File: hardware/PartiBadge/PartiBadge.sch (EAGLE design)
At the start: 20 parts, among them J1 I2C, J2 Supply

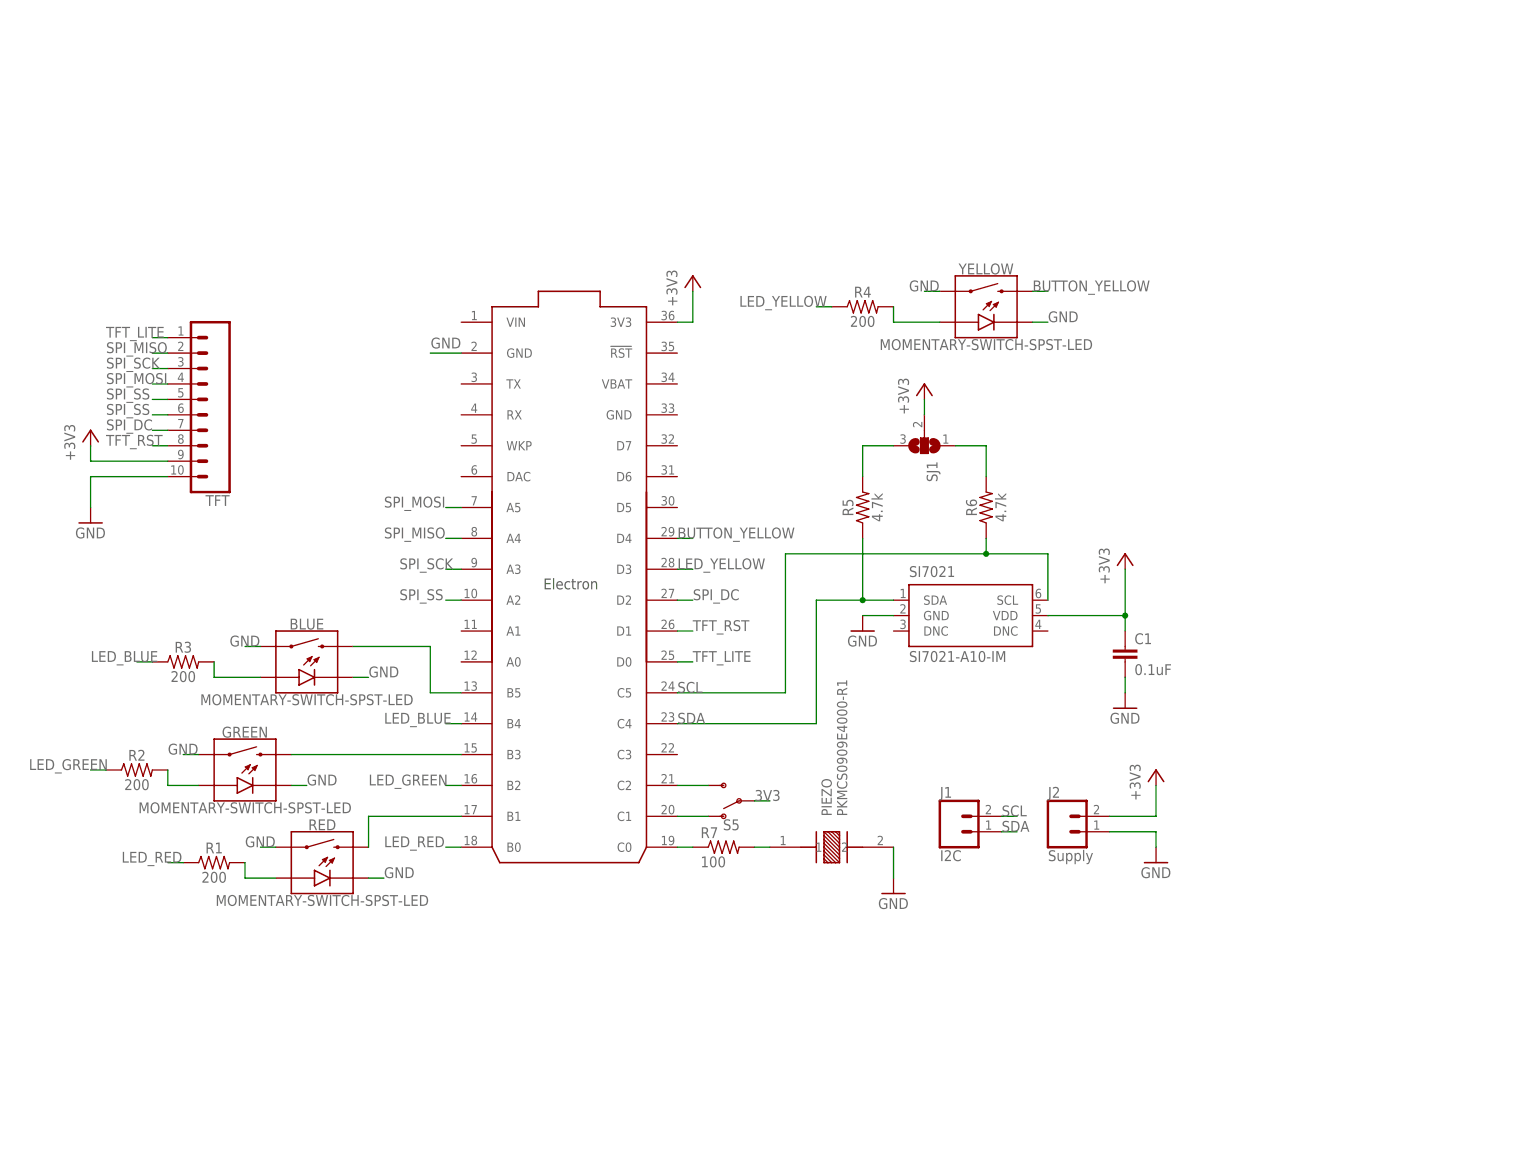
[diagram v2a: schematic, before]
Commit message: added frame and cleaned up schematic; added 5-way joystick
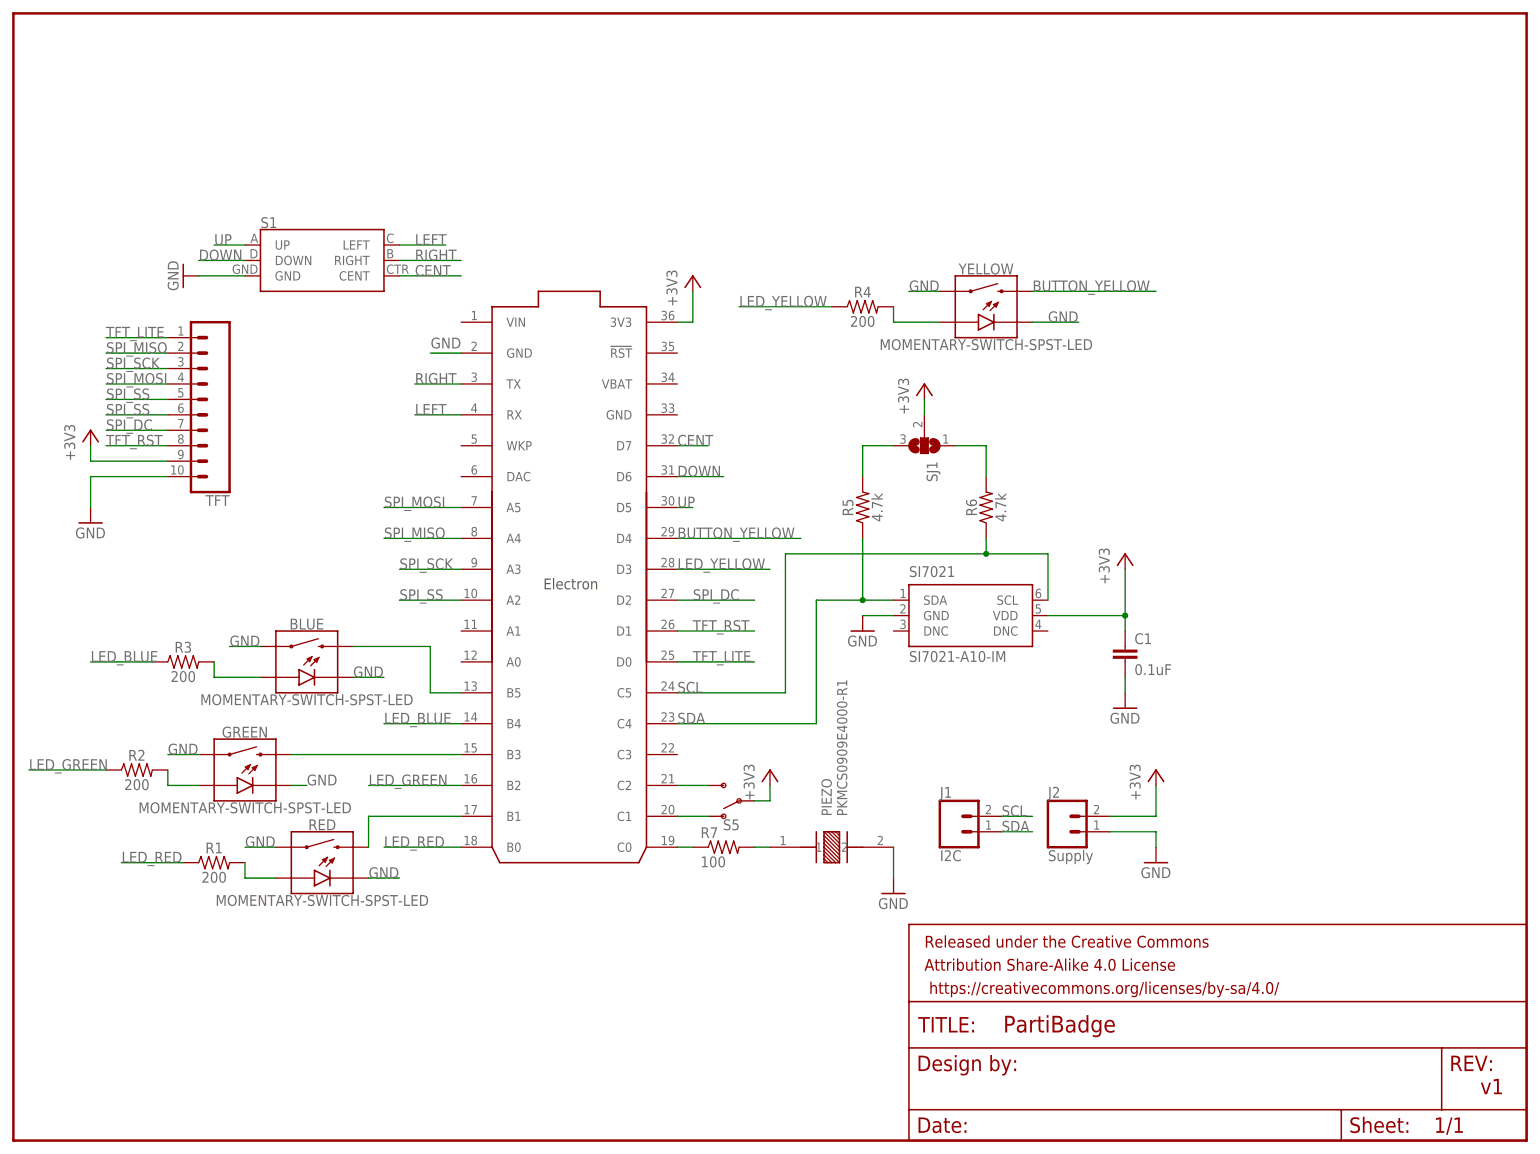
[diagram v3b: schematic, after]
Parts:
- added PARTIFRAME: FRAME-LETTERNO_PACKAGE, SparkFun-Aesthetics:FRAME-LETTERNO_PACKAGE
- added S1: (no value), SparkFun-Switches:JOYSTICK_MINI
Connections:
- new net CENT: ELECTRON.D7, S1.CENT
- new net DOWN: ELECTRON.D6, S1.DOWN
- new net LEFT: ELECTRON.RX, S1.LEFT
- new net RIGHT: ELECTRON.TX, S1.RIGHT
- new net UP: ELECTRON.D5, S1.UP
- net GND: now also S1.GND
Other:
- note added: "Brandon Satrom <brandon@particle.io>"
- note added: "v1"

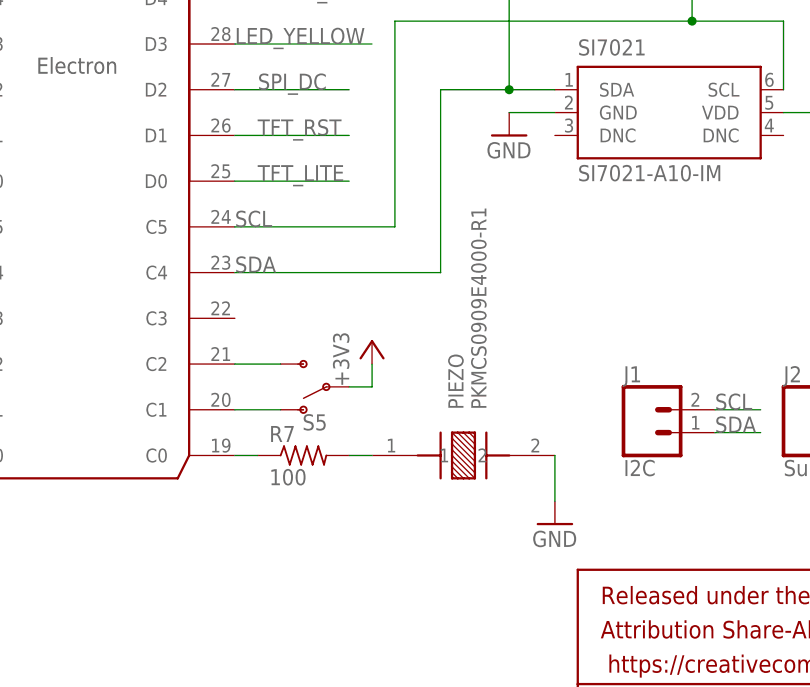
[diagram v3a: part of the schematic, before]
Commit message: Add clr to 3v3 line next to switch; closes #9; add text to back; closes #8
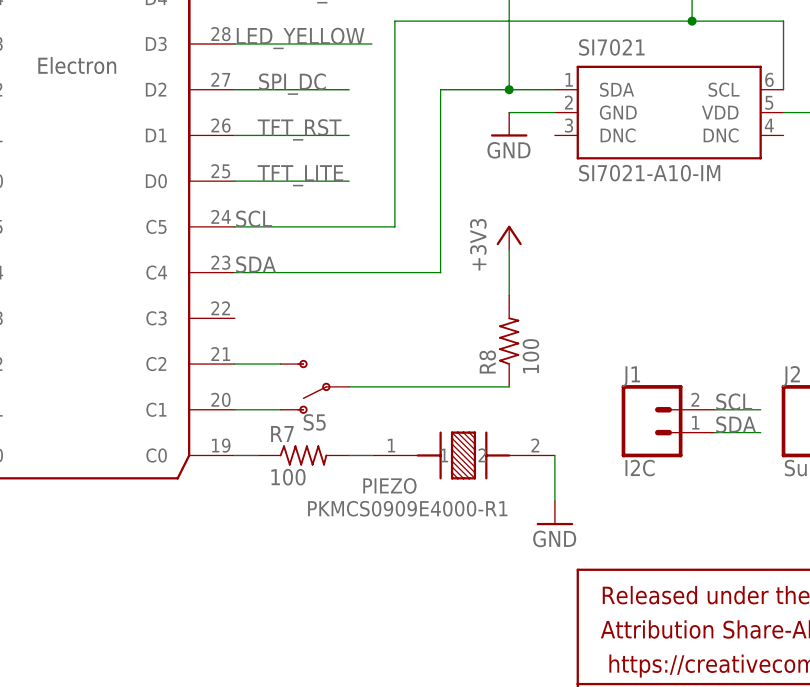
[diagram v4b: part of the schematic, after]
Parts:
- added R8: 100, rcl:R-US_M0805
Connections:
- net 3V3: now also R8.1, R8.2
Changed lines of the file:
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@@
 <attribute name="DESIGNER" value="Brandon Satrom"/>
 </part>
+<part name="R8" library="rcl" library_urn="urn:adsk.eagle:library:334" deviceset="R-US_" device="M0805" package3d_urn="urn:adsk.eagle:package:23556/1" value="100"/>
 </parts>
 <sheets>
@@
 <instance part="R3" gate="G$1" x="-33.02" y="38.1"/>
 <instance part="R4" gate="G$1" x="78.74" y="96.52"/>
-<instance part="PIEZO" gate="G$1" x="73.66" y="7.62" rot="R90"/>
+<instance part="PIEZO" gate="G$1" x="73.66" y="7.62" smashed="yes" rot="R90">
+<attribute name="NAME" x="68.561059375" y="5.08" size="1.68265" layer="95" rot="R180"/>
+<attribute name="VALUE" x="78.729109375" y="2.545440625" size="1.679990625" layer="96" rot="R180"/>
+</instance>
 <instance part="S5" gate="1" x="58.42" y="15.24" rot="R180"/>
 <instance part="R5" gate="G$1" x="78.74" y="63.5" rot="R90"/>
@@
 <instance part="S1" gate="G$1" x="-10.16" y="104.14"/>
 <instance part="GND6" gate="1" x="-33.02" y="101.6" rot="R270"/>
-<instance part="+3V6" gate="G$1" x="63.5" y="20.32"/>
+<instance part="+3V6" gate="G$1" x="78.74" y="33.02"/>
 <instance part="PARTIFRAME" gate="G$1" x="-60.96" y="-40.64" smashed="yes">
 <attribute name="DESIGNER" x="-60.96" y="-40.64" size="1.778" layer="96" display="off"/>
@@
 </instance>
 <instance part="PARTIFRAME" gate="V" x="86.36" y="-40.64"/>
+<instance part="R8" gate="G$1" x="78.74" y="20.32" rot="R90"/>
 </instances>
 <busses>
@@
 </segment>
 <segment>
+<pinref part="R8" gate="G$1" pin="2"/>
+<pinref part="+3V6" gate="G$1" pin="+3V3"/>
+<wire x1="78.74" y1="25.4" x2="78.74" y2="30.48" width="0.1524" layer="91"/>
+</segment>
+<segment>
 <pinref part="S5" gate="1" pin="P"/>
-<wire x1="60.96" y1="15.24" x2="63.5" y2="15.24" width="0.1524" layer="91"/>
-<pinref part="+3V6" gate="G$1" pin="+3V3"/>
-<wire x1="63.5" y1="15.24" x2="63.5" y2="17.78" width="0.1524" layer="91"/>
+<pinref part="R8" gate="G$1" pin="1"/>
+<wire x1="60.96" y1="15.24" x2="78.74" y2="15.24" width="0.1524" layer="91"/>
 </segment>
 </net>

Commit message: fix schematic and board with clr
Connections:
- new net N$14: R8.1, S5.P
- net 3V3: no longer R8.1, S5.P
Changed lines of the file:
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@@
 <wire x1="78.74" y1="25.4" x2="78.74" y2="30.48" width="0.1524" layer="91"/>
-</segment>
-<segment>
-<pinref part="S5" gate="1" pin="P"/>
-<pinref part="R8" gate="G$1" pin="1"/>
-<wire x1="60.96" y1="15.24" x2="78.74" y2="15.24" width="0.1524" layer="91"/>
 </segment>
 </net>
@@
 </segment>
 </net>
+<net name="N$14" class="0">
+<segment>
+<pinref part="S5" gate="1" pin="P"/>
+<pinref part="R8" gate="G$1" pin="1"/>
+<wire x1="60.96" y1="15.24" x2="78.74" y2="15.24" width="0.1524" layer="91"/>
+</segment>
+</net>

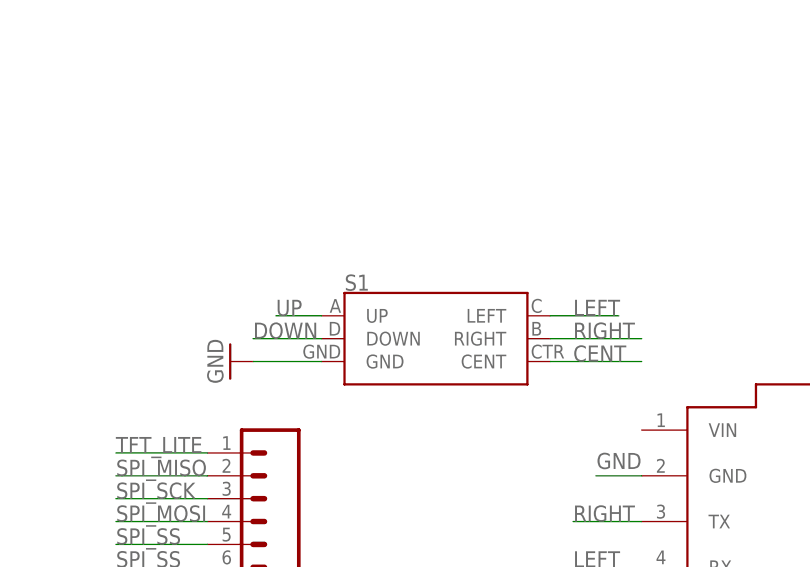
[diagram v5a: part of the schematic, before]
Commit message: smash ref designators and clean up refs; closes #14
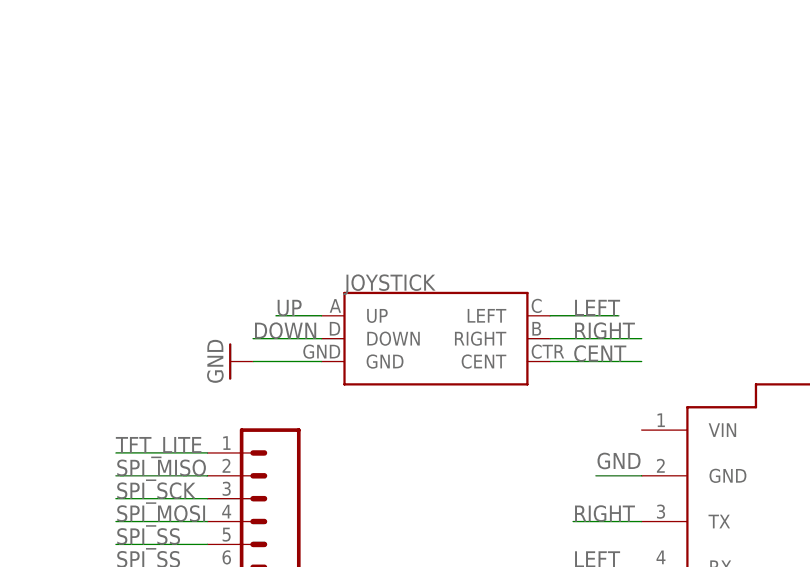
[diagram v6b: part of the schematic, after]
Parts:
- renumbered S1 to JOYSTICK
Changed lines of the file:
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@@
 <part name="J2" library="SparkFun-Connectors" library_urn="urn:adsk.eagle:library:513" deviceset="CONN_02" device="" package3d_urn="urn:adsk.eagle:package:38039/1" value="Supply"/>
 <part name="R7" library="rcl" library_urn="urn:adsk.eagle:library:334" deviceset="R-US_" device="M0805" package3d_urn="urn:adsk.eagle:package:23556/1" value="100"/>
-<part name="S1" library="SparkFun-Switches" library_urn="urn:adsk.eagle:library:535" deviceset="JOYSTICK_MINI" device="" package3d_urn="urn:adsk.eagle:package:40157/1"/>
+<part name="JOYSTICK" library="SparkFun-Switches" library_urn="urn:adsk.eagle:library:535" deviceset="JOYSTICK_MINI" device="" package3d_urn="urn:adsk.eagle:package:40157/1"/>
 <part name="GND6" library="supply1" library_urn="urn:adsk.eagle:library:371" deviceset="GND" device=""/>
 <part name="+3V6" library="supply1" library_urn="urn:adsk.eagle:library:371" deviceset="+3V3" device=""/>
@@
 <instance part="J2" gate="G$1" x="111.76" y="10.16"/>
 <instance part="R7" gate="G$1" x="55.88" y="7.62"/>
-<instance part="S1" gate="G$1" x="-10.16" y="104.14"/>
+<instance part="JOYSTICK" gate="G$1" x="-10.16" y="104.14"/>
 <instance part="GND6" gate="1" x="-33.02" y="101.6" rot="R270"/>
 <instance part="+3V6" gate="G$1" x="78.74" y="33.02"/>
@@
 </segment>
 <segment>
-<pinref part="S1" gate="G$1" pin="GND"/>
+<pinref part="JOYSTICK" gate="G$1" pin="GND"/>
 <pinref part="GND6" gate="1" pin="GND"/>
 <wire x1="-22.86" y1="101.6" x2="-30.48" y2="101.6" width="0.1524" layer="91"/>
@@
 <net name="UP" class="0">
 <segment>
-<pinref part="S1" gate="G$1" pin="UP"/>
+<pinref part="JOYSTICK" gate="G$1" pin="UP"/>
 <wire x1="-22.86" y1="106.68" x2="-27.94" y2="106.68" width="0.1524" layer="91"/>
 <label x="-27.94" y="106.68" size="1.778" layer="95"/>
@@
 <net name="DOWN" class="0">
 <segment>
-<pinref part="S1" gate="G$1" pin="DOWN"/>
+<pinref part="JOYSTICK" gate="G$1" pin="DOWN"/>
 <wire x1="-22.86" y1="104.14" x2="-30.48" y2="104.14" width="0.1524" layer="91"/>
 <label x="-30.48" y="104.14" size="1.778" layer="95"/>
@@
 <net name="LEFT" class="0">
 <segment>
-<pinref part="S1" gate="G$1" pin="LEFT"/>
+<pinref part="JOYSTICK" gate="G$1" pin="LEFT"/>
 <wire x1="2.54" y1="106.68" x2="10.16" y2="106.68" width="0.1524" layer="91"/>
 <label x="5.08" y="106.68" size="1.778" layer="95"/>
@@
 <net name="RIGHT" class="0">
 <segment>
-<pinref part="S1" gate="G$1" pin="RIGHT"/>
+<pinref part="JOYSTICK" gate="G$1" pin="RIGHT"/>
 <wire x1="2.54" y1="104.14" x2="12.7" y2="104.14" width="0.1524" layer="91"/>
 <label x="5.08" y="104.14" size="1.778" layer="95"/>
@@
 <net name="CENT" class="0">
 <segment>
-<pinref part="S1" gate="G$1" pin="CENT"/>
+<pinref part="JOYSTICK" gate="G$1" pin="CENT"/>
 <wire x1="2.54" y1="101.6" x2="12.7" y2="101.6" width="0.1524" layer="91"/>
 <label x="5.08" y="101.6" size="1.778" layer="95"/>
